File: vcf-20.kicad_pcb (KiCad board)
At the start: 2 copper layers, 30.5 x 110 mm, 119 parts, among them J1 IN1, J10 CV2, J2 IN2, J3 POWER, J4 HP, J5 LP, J6 BP, J7 NOTCH, J8 QCV, J9 CV1, Q1 BC858, Q2 BC858, Q3 BC858, U1 TL072, U2 LM13700, U3 TL074, U4 TL074, U5 TL074, U6 TL074, U7 TL074, U8 LM13700, U9 LM4040C5

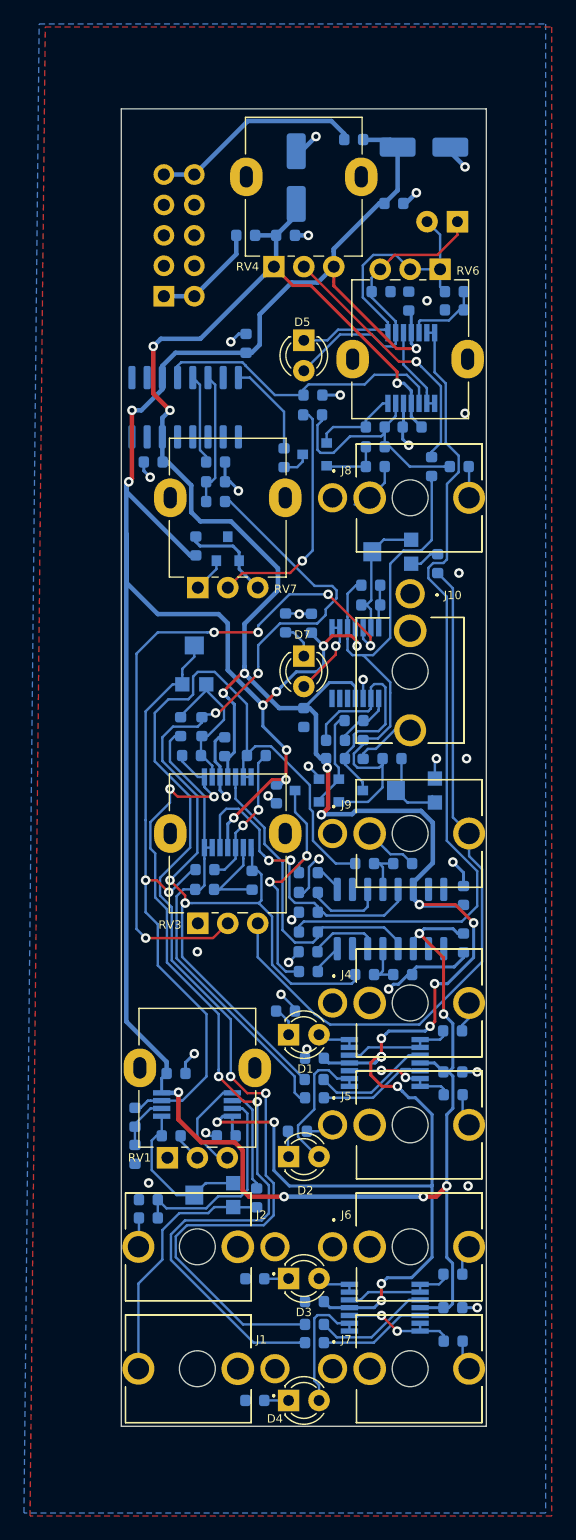
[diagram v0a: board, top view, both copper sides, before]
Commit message: Redesign filter core and revise board layout
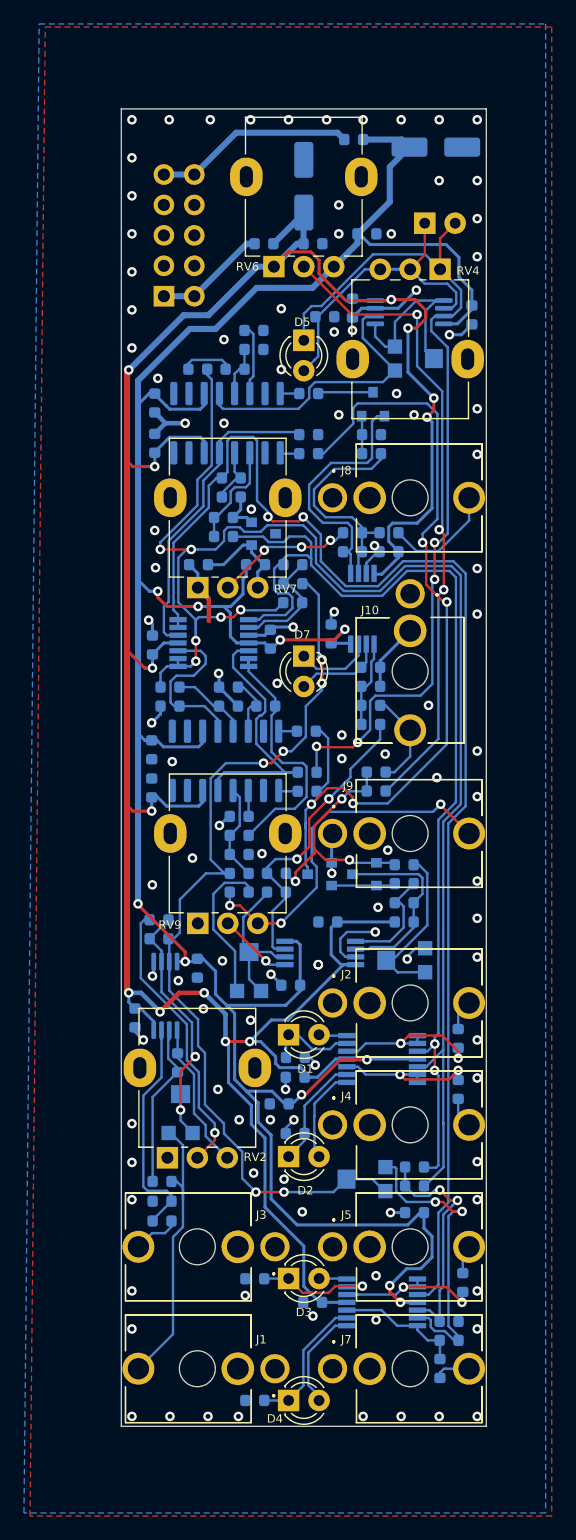
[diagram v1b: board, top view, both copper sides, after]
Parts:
- removed the C15 at (16.1, 90.9)
- removed the C16 at (16.1, 92.5)
- removed the C7 at (2.67, 39.4)
- removed the C9 at (10.4, 29.5)
- removed the R22 at (6.73, 61.5)
- removed the R23 at (4.95, 61.5)
- removed the R27 at (5.87, 63.9)
- removed the R3 at (2.26, 101.0)
- removed the R35 at (27.8, 26.7)
- removed the R36 at (27.8, 25.1)
- removed the R5 at (1.14, 97.2)
- removed the RV9 at (6.10, 56.1)
- removed the U1 at (6.32, 93.0)
- added C13: 1nF, Capacitor_SMD:C_0603_1608Metric, B.Cu at (15.6, 37.1)
- added C19: 100nF, Capacitor_SMD:C_0603_1608Metric, B.Cu at (2.79, 34.4)
- added C22: 100nF, Capacitor_SMD:C_0603_1608Metric, B.Cu at (22.4, 46.9)
- added C23: 100nF, Capacitor_SMD:C_0603_1608Metric, B.Cu at (17.5, 53.7)
- added C3: 100nF, Capacitor_SMD:C_0603_1608Metric, B.Cu at (6.45, 47.9)
- added R15: 10K, Resistor_SMD:R_0603_1608Metric, B.Cu at (27.4, 112.7)
- added R17: 10K, Resistor_SMD:R_0603_1608Metric, B.Cu at (24.5, 98.2)
- added R18: 10K, Resistor_SMD:R_0603_1608Metric, B.Cu at (27.4, 111.1)
- added R19: 10K, Resistor_SMD:R_0603_1608Metric, B.Cu at (24.5, 99.8)
- added R2: 10K, Resistor_SMD:R_0603_1608Metric, B.Cu at (4.70, 89.5)
- added R21: 10K, Resistor_SMD:R_0603_1608Metric, B.Cu at (9.18, 40.7)
- added R24: 10K, Resistor_SMD:R_0603_1608Metric, B.Cu at (15.6, 38.7)
- added R28: 10K, Resistor_SMD:R_0603_1608Metric, B.Cu at (8.53, 45.6)
- added R31: 220R, Resistor_SMD:R_0603_1608Metric, B.Cu at (8.53, 44.0)
- added R32: 220R, Resistor_SMD:R_0603_1608Metric, B.Cu at (9.18, 42.3)
- added R54: 1M, Resistor_SMD:R_0603_1608Metric, B.Cu at (20.8, 61.3)
- added R57: 1M, Resistor_SMD:R_0603_1608Metric, B.Cu at (20.8, 58.1)
- added R58: 1M, Resistor_SMD:R_0603_1608Metric, B.Cu at (20.8, 59.7)
- added R8: 10K, Resistor_SMD:R_0603_1608Metric, B.Cu at (3.40, 101.1)
- added RV3: 100K NOTCH DEPTH, Potentiometer_SMD:Potentiometer_Bourns_TC33X_Vertical, B.Cu at (20.3, 99.3)
- added RV5: B50K QDRIVE, Potentiometer_SMD:Potentiometer_Bourns_TC33X_Vertical, B.Cu at (24.6, 30.7)
- added U7: LM13700, Package_SO:SOIC-16_3.9x9.9mm_P1.27mm, B.Cu at (8.83, 36.1)
- added U9: TL072, Package_SO:TSSOP-8_4.4x3mm_P0.65mm, B.Cu at (20.1, 51.6)
- C18: value 0.47uF -> 100nF
- C27: renamed from C22; value 1nF -> 680pF
- R1: renamed from R11; value 2K -> 1K
- R11: renamed from R13; value 2K -> 1K
- R14: value 2K -> 1K
- R35: renamed from R42; value 33K -> 10K
- R36: renamed from R39; value 4.7K -> 1.8K
- R5: renamed from R12; value 2K -> 1K
- R55: renamed from R52; value 2K -> 1K
- RV4: renamed from RV6; value B50K QDRIVE -> 100K QFR
- RV8: renamed from RV5; value 1K TUNE -> 5K TUNE
- U10: renamed from U7; value TL074 -> TL072; footprint Package_SO:TSSOP-14_4.4x5mm_P0.65mm -> Package_SO:TSSOP-8_4.4x3mm_P0.65mm
- U2: value LM13700 -> TL072; footprint Package_SO:SOIC-16_3.9x9.9mm_P1.27mm -> Package_SO:TSSOP-8_4.4x3mm_P0.65mm
- U8: renamed from U6; value TL074 -> TL072; footprint Package_SO:TSSOP-14_4.4x5mm_P0.65mm -> Package_SO:TSSOP-8_4.4x3mm_P0.65mm
- moved C17 80.3 mm to (6.39, 31.6)
- moved C18 76.3 mm to (2.79, 37.8), turned to 90 degrees
- moved U2 49.2 mm to (3.68, 83.9)
- moved RV10 36.8 mm to (10.7, 81.7), turned to 90 degrees
- moved R52 32.0 mm to (9.84, 75.3), turned to 0 degrees
- moved C29 30.6 mm to (2.54, 63.4)
- moved C25 30.3 mm to (14.1, 83.1), turned to 180 degrees
- moved C28 27.5 mm to (2.54, 66.6)
- moved R47 27.5 mm to (21.3, 66.8), turned to 180 degrees
- moved R51 25.3 mm to (13.0, 73.7), turned to 0 degrees
- moved R53 25.2 mm to (13.0, 75.3)
- moved R37 25.0 mm to (14.3, 51.1), turned to 0 degrees
- moved U10 24.4 mm to (16.6, 80.4), turned to 180 degrees
- moved C12 20.7 mm to (4.06, 59.8)
- moved R30 19.6 mm to (8.95, 59.8)
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- renumbered C2 to C1, C13 to C10, C14 to C11, C21 to C12, C19 to C14, C23 to C15, C26 to C16, C5 to C2, C24 to C20, C27 to C21, C29 to C24, C30 to C25, C20 to C26, C25 to C28, C28 to C29, C3 to C4, C6 to C5, C1 to C6, C4 to C7, C10 to C8, C12 to C9, J4 to J2, J2 to J3, J5 to J4, J6 to J5, J3 to J6, R8 to R10, R9 to R12, R53 to R13, R10 to R16, R18 to R20, R15 to R22, R46 to R23, R34 to R25, R38 to R27, R41 to R29, R6 to R3, R40 to R30, R30 to R33, R31 to R34, R20 to R37, R21 to R38, R44 to R39, R7 to R4, R49 to R40, R48 to R41, R47 to R42, R37 to R43, R50 to R44, R43 to R46, R28 to R47, R32 to R48, R51 to R49, R33 to R50, R29 to R51, R17 to R52, R25 to R53, R16 to R56, R1 to R6, R2 to R7, R4 to R9, RV2 to RV1, RV8 to RV10, RV1 to RV2, RV4 to RV6, RV3 to RV9, U3 to U1, U4 to U3, U9 to U4, U8 to U6
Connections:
- C12 pad 1: Net-(C21-Pad1) -> Net-(C12-Pad1)
- C14 pad 1: Net-(C19-Pad1) -> Net-(C14-Pad1)
- C14 pad 2: Net-(C19-Pad2) -> Net-(C14-Pad2)
- C17 pad 1: Net-(C17-Pad1) -> /LP
- C17 pad 2: /FILTER/BP -> Net-(C17-Pad2)
- C18 pad 1: Net-(C18-Pad1) -> -12V
- C18 pad 2: /FILTER/NOTCH -> GND
- C26 pad 1: Net-(C20-Pad1) -> Net-(C26-Pad1)
- C26 pad 2: Net-(C20-Pad2) -> Net-(C26-Pad2)
- C27 pad 1: Net-(C22-Pad1) -> Net-(C27-Pad1)
- C27 pad 2: Net-(C22-Pad2) -> Net-(C27-Pad2)
- D5 pad 1: Net-(D5-Pad1) -> Net-(C14-Pad2)
- D6 pad 2: Net-(D5-Pad1) -> Net-(C14-Pad2)
- Q1 pad 3: Net-(C20-Pad2) -> Net-(C26-Pad2)
- Q3 pad 1: Net-(C22-Pad1) -> Net-(C27-Pad1)
- Q3 pad 3: Net-(Q3-Pad3) -> /FILTER/I_RES
- R1 pad 1: GND -> Net-(D1-Pad1)
- R1 pad 2: Net-(D1-Pad1) -> GND
- R16 pad 1: Net-(R10-Pad1) (its old number) -> Net-(R15-Pad2)
- R20 pad 1: Net-(R18-Pad1) -> Net-(R20-Pad1)
- R20 pad 2: /FILTER/HP -> /LP
- R22 pad 1: /FILTER/IN -> Net-(R22-Pad1)
- R22 pad 2: Net-(R15-Pad2) -> Net-(R22-Pad2)
- R23 pad 1: Net-(R46-Pad1) -> Net-(R23-Pad1)
- R25 pad 1: Net-(R34-Pad1) -> Net-(R25-Pad1)
- R26 pad 1: /FILTER/HP -> /IN
- R26 pad 2: Net-(R26-Pad2) -> Net-(R22-Pad1)
- R27 pad 1: /FILTER/BP -> Net-(R22-Pad2)
- R27 pad 2: Net-(R38-Pad2) -> Net-(R27-Pad2)
- R29 pad 1: Net-(R41-Pad1) -> Net-(R27-Pad2)
- R3 pad 1: Net-(R5-Pad1) -> Net-(R3-Pad1)
- R3 pad 2: /FILTER/IN -> /IN
- R30 pad 1: Net-(R38-Pad2) -> Net-(R20-Pad1)
- R33 pad 1: Net-(R26-Pad2) -> Net-(R22-Pad1)
- R34 pad 1: Net-(R31-Pad1) -> Net-(R34-Pad1)
- R35 pad 1: GND -> Net-(R35-Pad1)
- R35 pad 2: Net-(R42-Pad2) -> /HP
- R37 pad 1: Net-(R18-Pad1) -> /LP
- R37 pad 2: /FILTER/LP -> Net-(R35-Pad1)
- R38 pad 1: Net-(R15-Pad2) -> /IN
- R38 pad 2: /FILTER/BP -> Net-(R35-Pad1)
- R39 pad 1: Net-(R44-Pad1) -> /FILTER/I_RES
- R39 pad 2: Net-(Q3-Pad3) -> Net-(R39-Pad2)
- R40 pad 1: Net-(R48-Pad1) (its old number) -> Net-(R40-Pad1)
- R40 pad 2: /FILTER/HP -> Net-(C17-Pad2)
- R41 pad 1: Net-(R48-Pad1) (its old number) -> Net-(R40-Pad1)
- R42 pad 1: Net-(R47-Pad1) (its old number) -> Net-(R42-Pad1)
- R43 pad 1: Net-(C20-Pad1) -> Net-(C26-Pad1)
- R44 pad 1: Net-(C22-Pad2) -> Net-(C27-Pad2)
- R45 pad 2: Net-(C22-Pad2) -> Net-(C27-Pad2)
- R49 pad 1: Net-(C22-Pad2) -> Net-(C27-Pad2)
- R50 pad 2: Net-(C20-Pad2) -> Net-(C26-Pad2)
- R55 pad 1: GND -> Net-(D7-Pad2)
- R55 pad 2: Net-(D7-Pad1) -> GND
- R6 pad 1: Net-(R1-Pad1) -> Net-(R2-Pad2)
- R7 pad 1: Net-(R2-Pad1) -> Net-(R7-Pad1)
- R9 pad 2: Net-(R4-Pad2) -> Net-(R3-Pad1)
- RV1 pad 1: Net-(R4-Pad2) -> Net-(R3-Pad1)
- RV1 pad 2: Net-(R4-Pad2) -> Net-(R3-Pad1)
- RV2 pad 3: Net-(RV1-Pad3) -> Net-(R2-Pad1)
- RV4 pad 1: Net-(D5-Pad1) -> Net-(C14-Pad2)
- RV4 pad 2: Net-(D5-Pad1) -> Net-(D5-Pad2)
- U1 pad 13: Net-(D1-Pad2) -> Net-(D1-Pad1)
- U1 pad 3: Net-(C15-Pad1) -> /HP
- U1 pad 5: Net-(C16-Pad1) -> /LP
- U1 pad 9: Net-(D2-Pad2) -> Net-(D2-Pad1)
- U10 pad 1: Net-(D7-Pad2) -> Net-(C26-Pad1)
- U10 pad 2: Net-(D7-Pad2) -> Net-(C26-Pad2)
- U10 pad 3: Net-(Q1-Pad1) -> GND
- U10 pad 4: +12V -> -12V
- U10 pad 8: Net-(C20-Pad1) -> +12V
- U2 pad 1: (no net) -> Net-(R2-Pad1)
- U2 pad 2: (no net) -> Net-(R2-Pad2)
- U2 pad 3: (no net) -> Net-(R7-Pad1)
- U2 pad 4: (no net) -> -12V
- U2 pad 5: (no net) -> GND
- U2 pad 6: -12V -> Net-(R3-Pad1)
- U2 pad 7: (no net) -> /IN
- U2 pad 8: (no net) -> +12V
- U3 pad 10: Net-(R10-Pad1) (its old number) -> Net-(R15-Pad2)
- U3 pad 13: Net-(D3-Pad2) -> Net-(D3-Pad1)
- U3 pad 3: Net-(C17-Pad1) -> /FILTER/BP
- U3 pad 5: Net-(C18-Pad1) -> Net-(R17-Pad2)
- U3 pad 6: Net-(R10-Pad1) (its old number) -> Net-(R15-Pad1)
- U3 pad 7: Net-(R10-Pad1) (its old number) -> Net-(R15-Pad2)
- U3 pad 9: Net-(D4-Pad2) -> Net-(D4-Pad1)
- U5 pad 1: /FILTER/HP -> /HP
- U5 pad 10: GND -> Net-(C12-Pad1)
- U5 pad 12: Net-(C19-Pad1) -> Net-(C13-Pad1)
- U5 pad 2: Net-(R18-Pad1) -> Net-(R35-Pad1)
- U5 pad 3: Net-(R15-Pad2) -> GND
- U5 pad 5: Net-(C21-Pad1) -> Net-(C14-Pad1)
- U5 pad 6: /FILTER/LP -> Net-(R22-Pad2)
- U5 pad 7: /FILTER/LP -> Net-(R22-Pad2)
- U5 pad 8: /FILTER/NOTCH -> /LP
- U5 pad 9: Net-(R22-Pad2) -> /LP
- U6 pad 1: Net-(R46-Pad1) -> Net-(R25-Pad1)
- U6 pad 12: Net-(C19-Pad1) -> Net-(C12-Pad1)
- U6 pad 13: Net-(R26-Pad2) -> Net-(R20-Pad1)
- U6 pad 14: Net-(R31-Pad1) -> Net-(R27-Pad2)
- U6 pad 16: Net-(R34-Pad1) -> Net-(R23-Pad1)
- U6 pad 3: Net-(R41-Pad1) -> Net-(R34-Pad1)
- U6 pad 4: Net-(R38-Pad2) -> Net-(R22-Pad1)
- U6 pad 5: Net-(C21-Pad1) -> Net-(C14-Pad1)
- U8 pad 1: Net-(D5-Pad1) -> Net-(RV5-Pad2)
- U8 pad 2: Net-(D5-Pad2) -> Net-(RV5-Pad1)
- U8 pad 3: Net-(U6-Pad3) -> GND
- U8 pad 4: +12V -> -12V
- U8 pad 5: Net-(R35-Pad1) -> Net-(RV5-Pad2)
- U8 pad 6: Net-(C19-Pad2) -> Net-(D5-Pad2)
- U8 pad 7: Net-(C19-Pad2) -> Net-(C14-Pad2)
- U8 pad 8: Net-(U6-Pad3) -> +12V
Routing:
- net /LP: track 0.00 -> 129.0 mm, vias 0 -> 6
- net /FILTER/HP: track 95.2 -> 0.00 mm, vias 4 -> 0
- net /HP: track 0.00 -> 88.7 mm, vias 0 -> 2
- net /IN: track 0.00 -> 77.3 mm, vias 0 -> 6
- net /FILTER/NOTCH: track 74.8 -> 0.00 mm, vias 4 -> 0
- net Net-(C14-Pad2): track 0.00 -> 74.6 mm, vias 0 -> 4
- net Net-(C19-Pad2): track 68.7 -> 0.00 mm
- net /FILTER/IN: track 52.7 -> 0.00 mm, vias 2 -> 0
- net Net-(RV9-Pad2): track 57.4 -> 6.20 mm, vias 5 -> 1
- net /FILTER/I_ABC: track 20.7 -> 70.7 mm, vias 2 -> 4
- net /FILTER/LP: track 39.2 -> 0.00 mm
- net Net-(R47-Pad1): track 21.8 -> 54.1 mm, vias 1 -> 3
- net Net-(J9-Pad3): track 60.0 -> 30.4 mm, vias 0 -> 3
- net Net-(D5-Pad1): track 27.8 -> 0.00 mm
- net Net-(C19-Pad1): track 27.4 -> 0.00 mm
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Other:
- board text added: "github.com/covertneko/vcf-20 /tree/v0.2"
- board text removed: "github.com/covertneko/vcf-20/tree/v0.1"

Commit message: Add panel, plus some minor fixes to crossfade and resonance drive
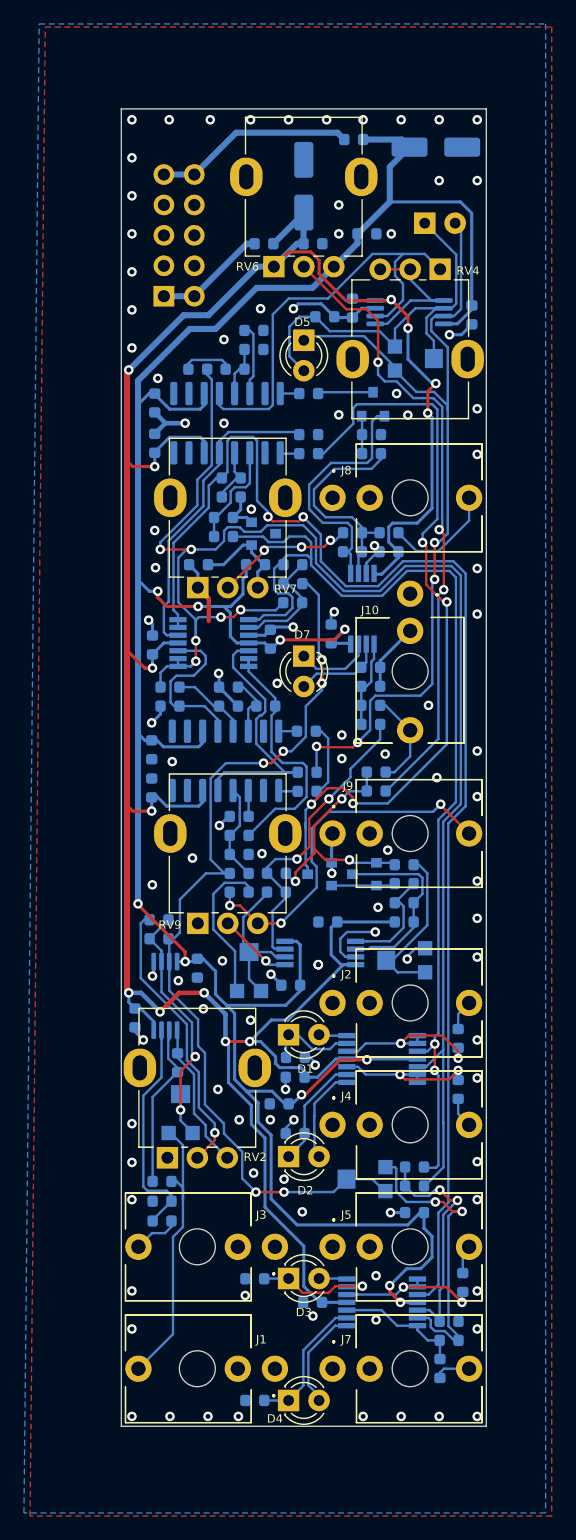
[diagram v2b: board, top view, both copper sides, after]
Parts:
- RV4: value 100K QFR -> B50K QDRIVE
- RV5: value B50K QDRIVE -> 100K QFR
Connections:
- RV4 pad 1: Net-(C14-Pad2) -> Net-(RV4-Pad1)
- RV4 pad 2: Net-(D5-Pad2) -> Net-(RV4-Pad2)
- RV4 pad 3: Net-(D5-Pad2) -> Net-(RV4-Pad2)
- RV5 pad 1: Net-(RV5-Pad1) -> Net-(C14-Pad2)
- RV5 pad 2: Net-(RV5-Pad2) -> Net-(D5-Pad2)
- RV5 pad 3: Net-(RV5-Pad2) -> Net-(D5-Pad2)
- U7 pad 12: Net-(RV5-Pad1) -> Net-(RV4-Pad1)
- U8 pad 1: Net-(RV5-Pad2) -> Net-(RV4-Pad2)
- U8 pad 2: Net-(RV5-Pad1) -> Net-(RV4-Pad1)
- U8 pad 5: Net-(RV5-Pad2) -> Net-(RV4-Pad2)
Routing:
- net Net-(RV4-Pad1): track 0.00 -> 37.1 mm
- net Net-(RV5-Pad1): track 24.1 -> 0.00 mm
- net Net-(RV5-Pad2): track 16.2 -> 0.00 mm
- net Net-(RV4-Pad2): track 0.00 -> 13.4 mm
- net Net-(D5-Pad2): track 25.7 -> 35.3 mm
- net -12V: track 228.8 -> 226.3 mm
- net Net-(C14-Pad2): track 74.6 -> 72.5 mm
- net GND: track 63.3 -> 64.8 mm, vias 112 -> 107
- net +12V: track 229.2 -> 230.4 mm
- net Net-(R47-Pad1): track 54.1 -> 53.4 mm
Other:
- board text added: "github.com/covertneko/vcf-20 /tree/v0.2.1"
- board text removed: "github.com/covertneko/vcf-20 /tree/v0.2"
